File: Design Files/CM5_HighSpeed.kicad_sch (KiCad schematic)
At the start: 8 parts, among them J11 Conn_01x04_MountingPin, J2 HDMI_A_1.4, U17 RT9742SNGV

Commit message: More interface interconnects
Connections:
- net +5v renamed 5V0_Peripheral
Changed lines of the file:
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@@
 		)
 	)
-	(hierarchical_label "+5v"
+	(hierarchical_label "5V0_Peripheral"
 		(shape input)
 		(at 273.05 185.42 180)
@@
 		)
 	)
-	(hierarchical_label "+5v"
+	(hierarchical_label "5V0_Peripheral"
 		(shape input)
 		(at 218.44 130.81 0)

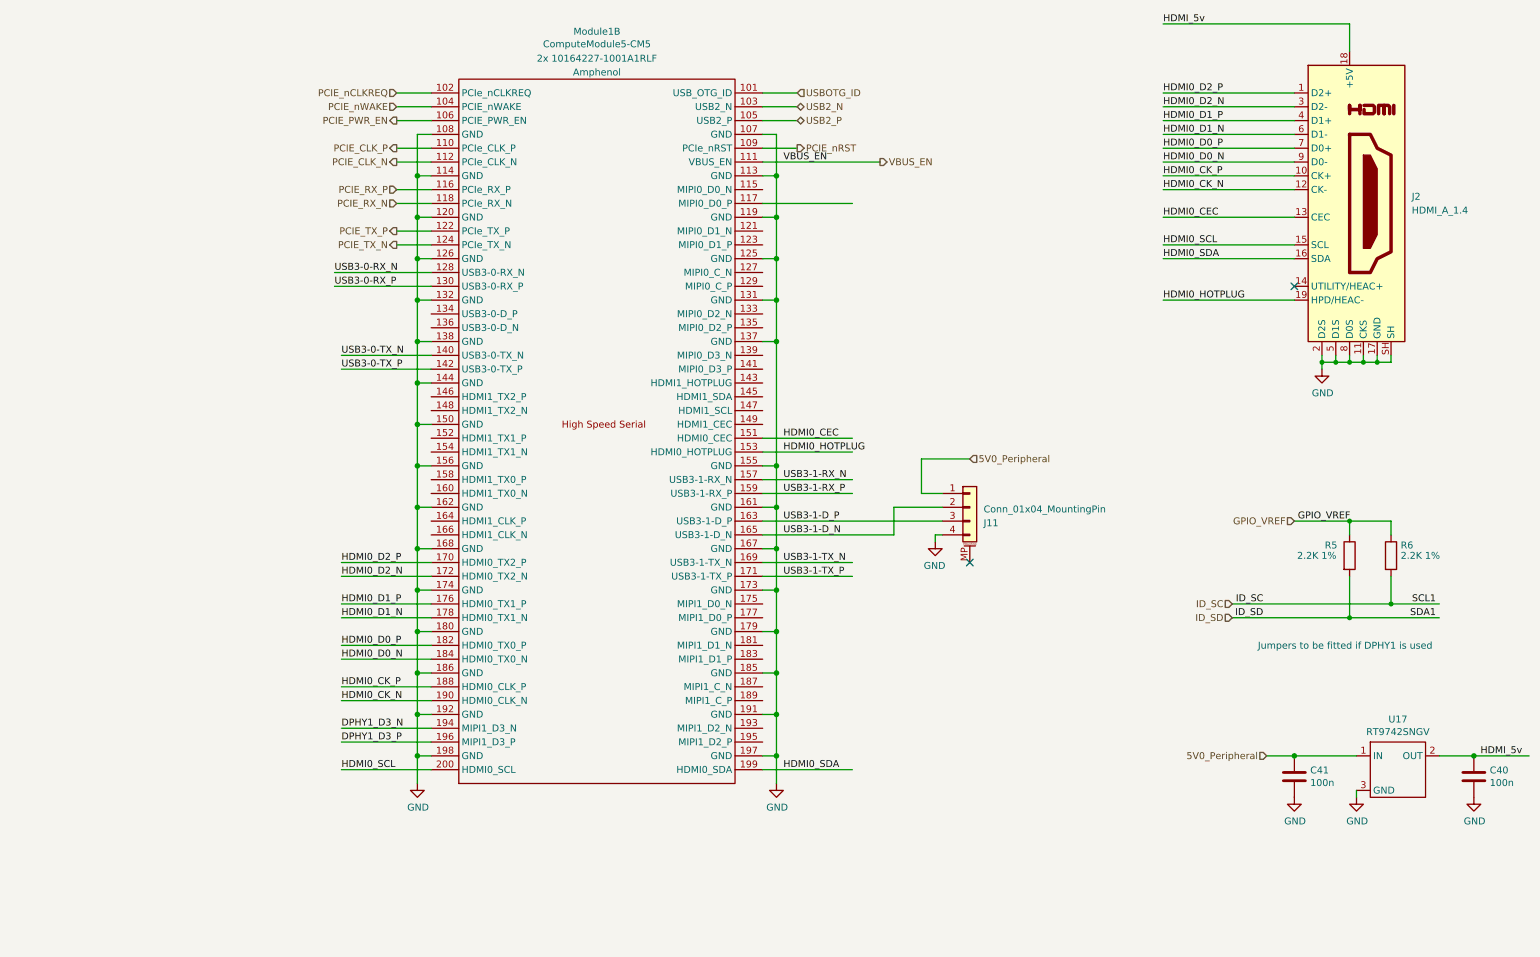
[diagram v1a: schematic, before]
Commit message: Fixed power & GPIO nets
Added PWM I2C Bus
Replaced global power labels on the sensor page with hierarchical pins & page labels
Cleaned up CM5 GPIO block sheet
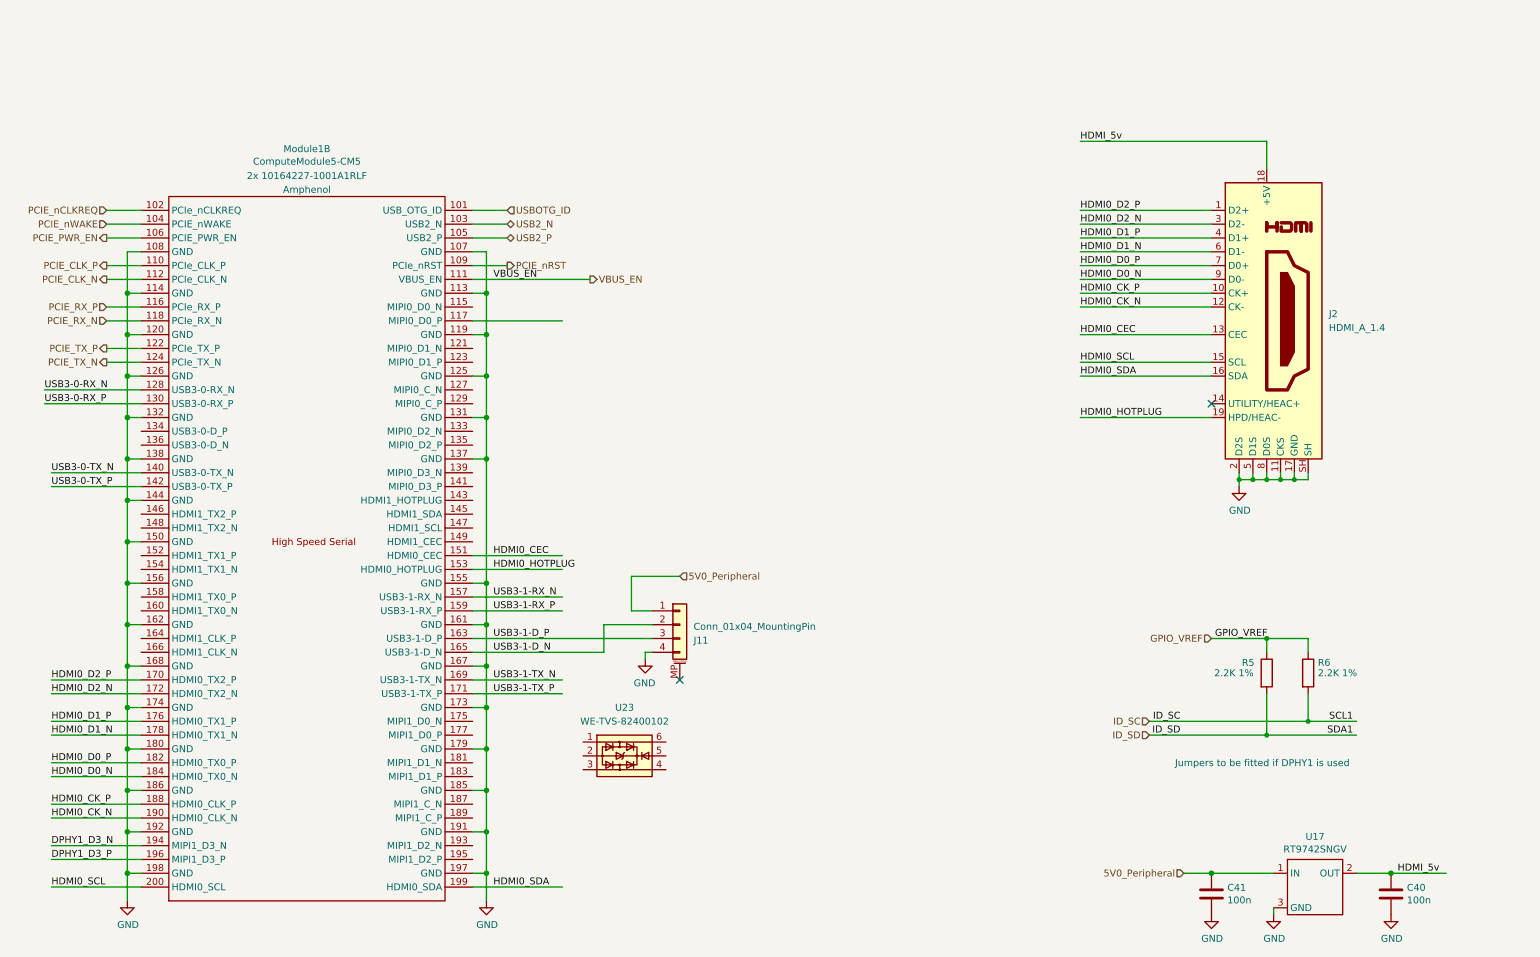
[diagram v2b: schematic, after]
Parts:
- added U23: WE-TVS-82400102, Package_TO_SOT_SMD:SOT-23-6, symbol Power_Protection:WE-TVS-82400102
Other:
- moved on the sheet: C40, C41, J11, J2, Module1B, R5, R6, U17

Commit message: Misc
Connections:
- net USB3-1-D_N: now also U23.1; no longer J11.2 (Pin_2)
- net USB3-1-D_P: now also U23.3; no longer J11.3 (Pin_3)
- net at U23.4: now also J11.3 (Pin_3)
- net at U23.6: now also J11.2 (Pin_2)
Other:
- note removed: "Jumpers to be fitted if DPHY1 is used"
- moved on the sheet: J11, U23
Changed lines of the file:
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@@
 		(comment 3 "https://github.com/loganrf/compactPi")
 	)
-	(text "Jumpers to be fitted if DPHY1 is used\n"
-		(exclude_from_sim no)
-		(at 288.29 187.706 0)
-		(effects
-			(font
-				(size 1.27 1.27)
-			)
-			(justify right bottom)
-		)
-	)
 	(junction
 		(at 273.05 163.83)
@@
 	)
 	(no_connect
-		(at 165.1 171.45)
+		(at 207.01 163.83)
+	)
+	(wire
+		(pts
+			(xy 194.31 157.48) (xy 189.23 157.48)
+		)
+		(stroke
+			(width 0)
+			(type default)
+		)
 	)
 	(wire
@@
 	(wire
 		(pts
+			(xy 194.31 156.21) (xy 194.31 157.48)
+		)
+		(stroke
+			(width 0)
+			(type default)
+		)
+	)
+	(wire
+		(pts
 			(xy 273.05 163.83) (xy 280.67 163.83)
 		)
@@
 	(wire
 		(pts
+			(xy 189.23 152.4) (xy 193.04 152.4)
+		)
+		(stroke
+			(width 0)
+			(type default)
+		)
+	)
+	(wire
+		(pts
 			(xy 238.76 95.25) (xy 262.89 95.25)
 		)
@@
 	(wire
 		(pts
-			(xy 165.1 152.4) (xy 156.21 152.4)
+			(xy 207.01 144.78) (xy 198.12 144.78)
 		)
 		(stroke
@@
 	(wire
 		(pts
+			(xy 193.04 153.67) (xy 201.93 153.67)
+		)
+		(stroke
+			(width 0)
+			(type default)
+		)
+	)
+	(wire
+		(pts
 			(xy 278.13 133.35) (xy 278.13 134.62)
 		)
@@
 	(wire
 		(pts
-			(xy 156.21 158.75) (xy 160.02 158.75)
+			(xy 198.12 151.13) (xy 201.93 151.13)
 		)
 		(stroke
@@
 	(wire
 		(pts
-			(xy 156.21 152.4) (xy 156.21 158.75)
+			(xy 198.12 144.78) (xy 198.12 151.13)
+		)
+		(stroke
+			(width 0)
+			(type default)
+		)
+	)
+	(wire
+		(pts
+			(xy 201.93 156.21) (xy 194.31 156.21)
 		)
 		(stroke
@@
 	(wire
 		(pts
+			(xy 173.99 157.48) (xy 173.99 163.83)
+		)
+		(stroke
+			(width 0)
+			(type default)
+		)
+	)
+	(wire
+		(pts
 			(xy 270.51 134.62) (xy 267.97 134.62)
 		)
@@
 	(wire
 		(pts
+			(xy 170.18 152.4) (xy 170.18 161.29)
+		)
+		(stroke
+			(width 0)
+			(type default)
+		)
+	)
+	(wire
+		(pts
+			(xy 173.99 152.4) (xy 170.18 152.4)
+		)
+		(stroke
+			(width 0)
+			(type default)
+		)
+	)
+	(wire
+		(pts
 			(xy 63.5 153.67) (xy 66.04 153.67)
 		)
@@
 	(wire
 		(pts
-			(xy 158.75 166.37) (xy 158.75 167.64)
+			(xy 200.66 158.75) (xy 200.66 160.02)
 		)
 		(stroke
@@
 	(wire
 		(pts
-			(xy 151.13 161.29) (xy 160.02 161.29)
+			(xy 151.13 161.29) (xy 170.18 161.29)
 		)
 		(stroke
@@
 	(wire
 		(pts
-			(xy 127 163.83) (xy 160.02 163.83)
+			(xy 127 163.83) (xy 173.99 163.83)
 		)
 		(stroke
@@
 	(wire
 		(pts
+			(xy 193.04 152.4) (xy 193.04 153.67)
+		)
+		(stroke
+			(width 0)
+			(type default)
+		)
+	)
+	(wire
+		(pts
 			(xy 127 166.37) (xy 151.13 166.37)
 		)
@@
 	(wire
 		(pts
-			(xy 160.02 166.37) (xy 158.75 166.37)
+			(xy 201.93 158.75) (xy 200.66 158.75)
 		)
 		(stroke
@@
 		)
 	)
-	(label "USB3-1-D_N"
-		(at 130.81 166.37 0)
-		(effects
-			(font
-				(size 1.27 1.27)
-			)
-			(justify left bottom)
-		)
-	)
 	(label "HDMI0_D1_N"
 		(at 238.76 92.71 0)
@@
 		)
 	)
+	(label "USB3-1-D_N"
+		(at 156.21 161.29 0)
+		(effects
+			(font
+				(size 1.27 1.27)
+			)
+			(justify left bottom)
+		)
+	)
 	(label "HDMI0_D2_N"
 		(at 238.76 87.63 0)
@@
 	)
 	(label "USB3-1-D_P"
-		(at 130.81 163.83 0)
+		(at 168.91 163.83 180)
 		(effects
 			(font
 				(size 1.27 1.27)
 			)
-			(justify left bottom)
+			(justify right bottom)
 		)
 	)
@@
 	(hierarchical_label "5V0_Peripheral"
 		(shape input)
-		(at 165.1 152.4 0)
+		(at 207.01 144.78 0)
 		(effects
 			(font
@@
 	(symbol
 		(lib_id "power:GND")
-		(at 158.75 167.64 0)
+		(at 200.66 160.02 0)
 		(mirror y)
 		(unit 1)
@@
 		(dnp no)
 		(property "Reference" "#PWR08"
-			(at 158.75 173.99 0)
+			(at 200.66 166.37 0)
 			(hide yes)
 			(show_name no)
@@
 		)
 		(property "Value" "GND"
-			(at 158.623 172.0342 0)
+			(at 200.533 164.4142 0)
 			(show_name no)
 			(do_not_autoplace no)
@@
 		)
 		(property "Footprint" ""
-			(at 158.75 167.64 0)
+			(at 200.66 160.02 0)
 			(hide yes)
 			(show_name no)
@@
 		)
 		(property "Datasheet" ""
-			(at 158.75 167.64 0)
+			(at 200.66 160.02 0)
 			(hide yes)
 			(show_name no)
@@
 		)
 		(property "Description" "Power symbol creates a global label with name \"GND\" , ground"
-			(at 158.75 167.64 0)
+			(at 200.66 160.02 0)
 			(hide yes)
 			(show_name no)
@@
 	(symbol
 		(lib_id "Connector_Generic_MountingPin:Conn_01x04_MountingPin")
-		(at 165.1 161.29 0)
+		(at 207.01 153.67 0)
 		(unit 1)
 		(body_style 1)
@@
 		(dnp no)
 		(property "Reference" "J11"
-			(at 167.64 164.1857 0)
+			(at 209.55 156.5657 0)
 			(show_name no)
 			(do_not_autoplace no)
@@
 		)
 		(property "Value" "Conn_01x04_MountingPin"
-			(at 167.64 161.6457 0)
+			(at 209.55 154.0257 0)
 			(show_name no)
 			(do_not_autoplace no)
@@
 		)
 		(property "Footprint" "Connector_JST:JST_GH_BM04B-GHS-TBT_1x04-1MP_P1.25mm_Vertical"
-			(at 165.1 161.29 0)
+			(at 207.01 153.67 0)
 			(hide yes)
 			(show_name no)
@@
 		)
 		(property "Datasheet" ""
-			(at 165.1 161.29 0)
+			(at 207.01 153.67 0)
 			(hide yes)
 			(show_name no)
@@
 		)
 		(property "Description" "Generic connectable mounting pin connector, single row, 01x04, script generated (kicad-library-utils/schlib/autogen/connector/)"
-			(at 165.1 161.29 0)
+			(at 207.01 153.67 0)
 			(hide yes)
 			(show_name no)
@@
 	(symbol
 		(lib_id "Power_Protection:WE-TVS-82400102")
-		(at 154.94 185.42 0)
+		(at 181.61 154.94 0)
 		(unit 1)
 		(body_style 1)
@@
 		(fields_autoplaced yes)
 		(property "Reference" "U23"
-			(at 154.94 176.53 0)
+			(at 181.61 146.05 0)
 			(show_name no)
 			(do_not_autoplace no)
@@
 		)
 		(property "Value" "WE-TVS-82400102"
-			(at 154.94 179.07 0)
+			(at 181.61 148.59 0)
 			(show_name no)
 			(do_not_autoplace no)
@@
 		)
 		(property "Footprint" "Package_TO_SOT_SMD:SOT-23-6"
-			(at 154.94 190.5 0)
+			(at 181.61 160.02 0)
 			(hide yes)
 			(show_name no)
@@
 		)
 		(property "Datasheet" "https://www.we-online.com/components/products/datasheet/82400102.pdf"
-			(at 154.94 191.77 0)
+			(at 181.61 161.29 0)
 			(hide yes)
 			(show_name no)
@@
 		)
 		(property "Description" "Low Capacitance TVS Diode Array, 2 Channels, SOT-23-6"
-			(at 154.94 185.42 0)
+			(at 181.61 154.94 0)
 			(hide yes)
 			(show_name no)
